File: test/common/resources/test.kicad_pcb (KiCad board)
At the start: 2 copper layers, 3 parts

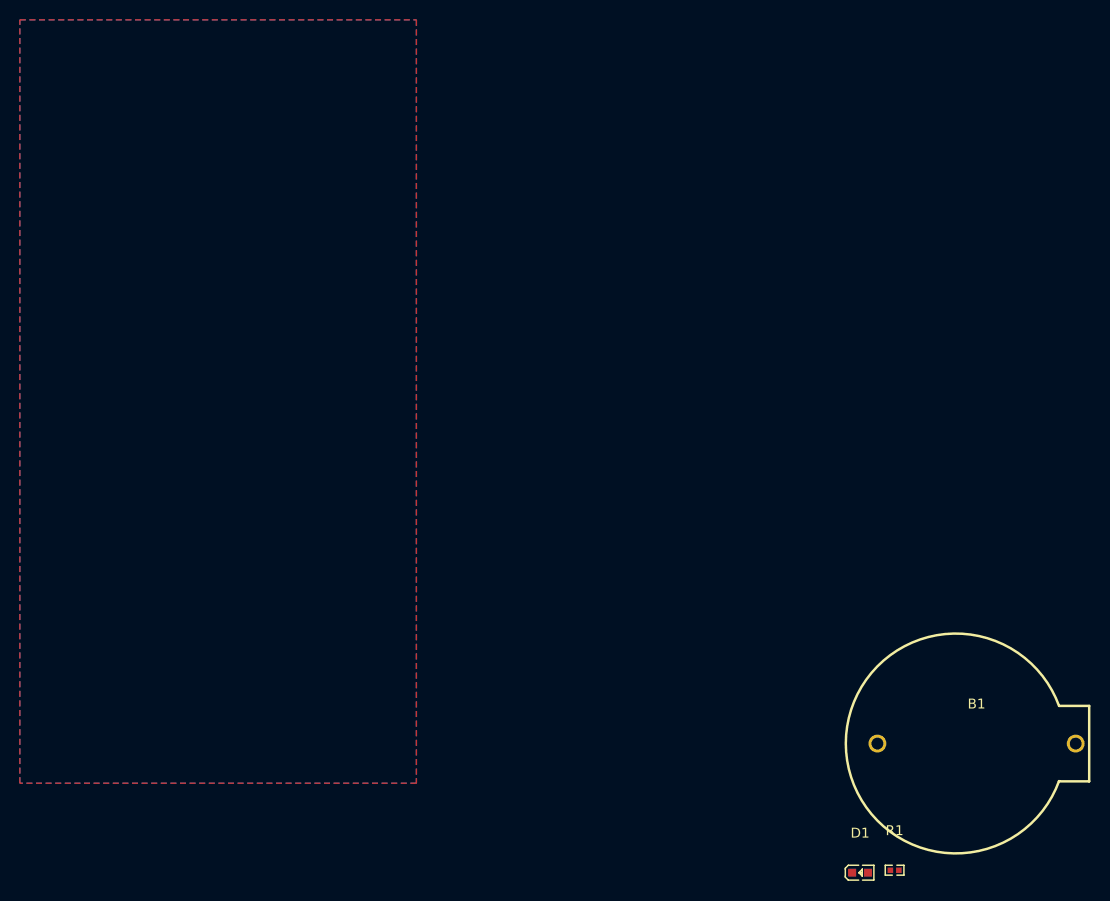
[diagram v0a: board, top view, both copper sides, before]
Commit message: Add: keepout zone to test pcb file
Auto formatted by KiCad
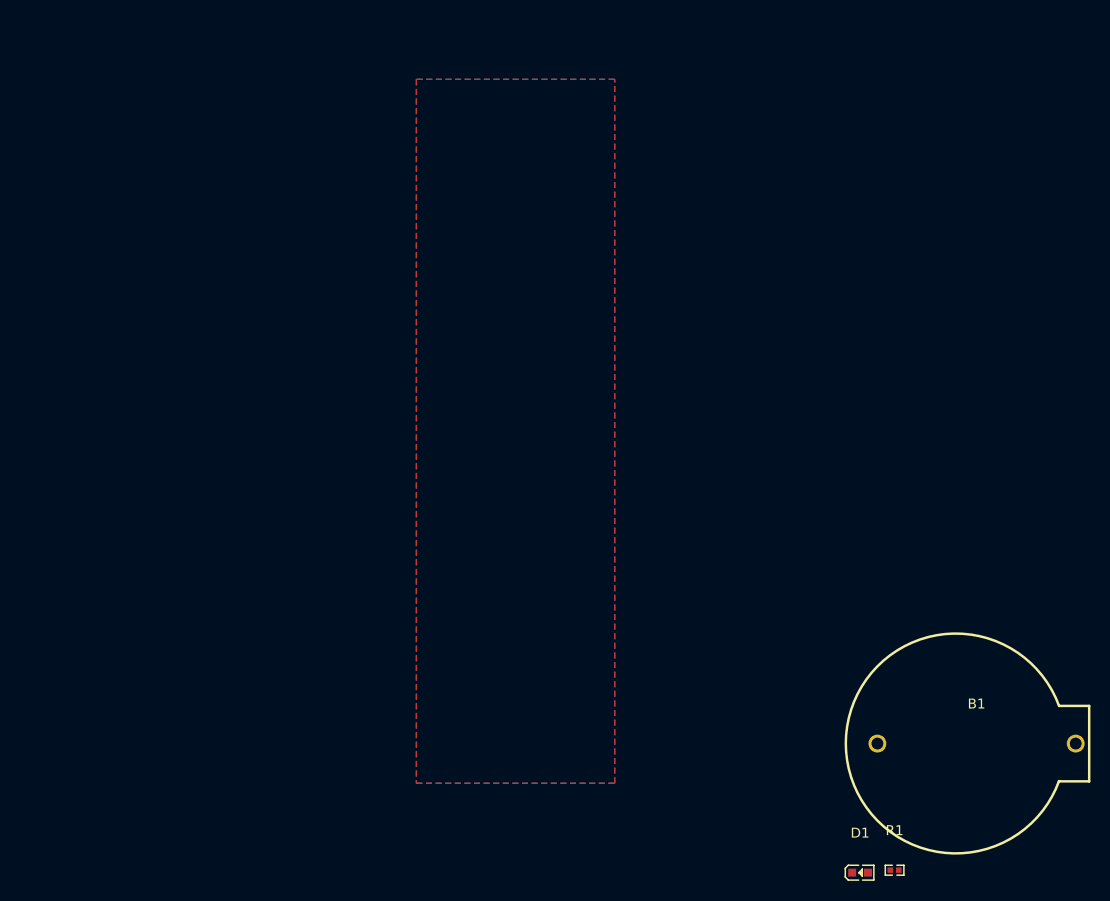
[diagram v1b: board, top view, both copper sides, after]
